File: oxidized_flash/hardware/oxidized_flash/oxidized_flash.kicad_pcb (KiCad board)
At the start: 2 copper layers, 61 x 21.6 mm, 20 parts, among them J1 USB_A, J2 Conn_ARM_JTAG_SWD_10, U1 LM1117-3.3, U2 ATSAMD51G18A-MU, U3 MT25QL

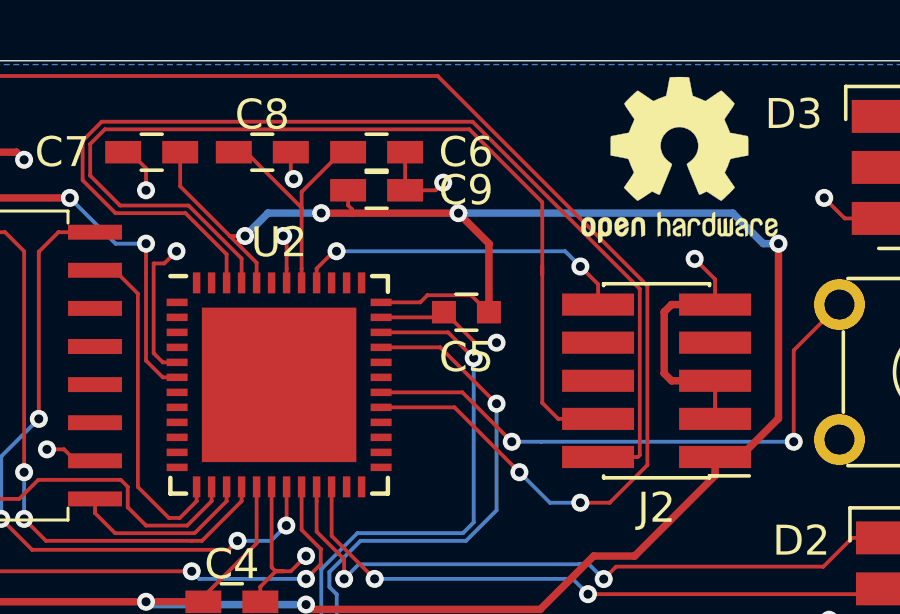
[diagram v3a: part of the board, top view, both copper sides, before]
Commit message: Update C5 to use a hand-soldered footprint
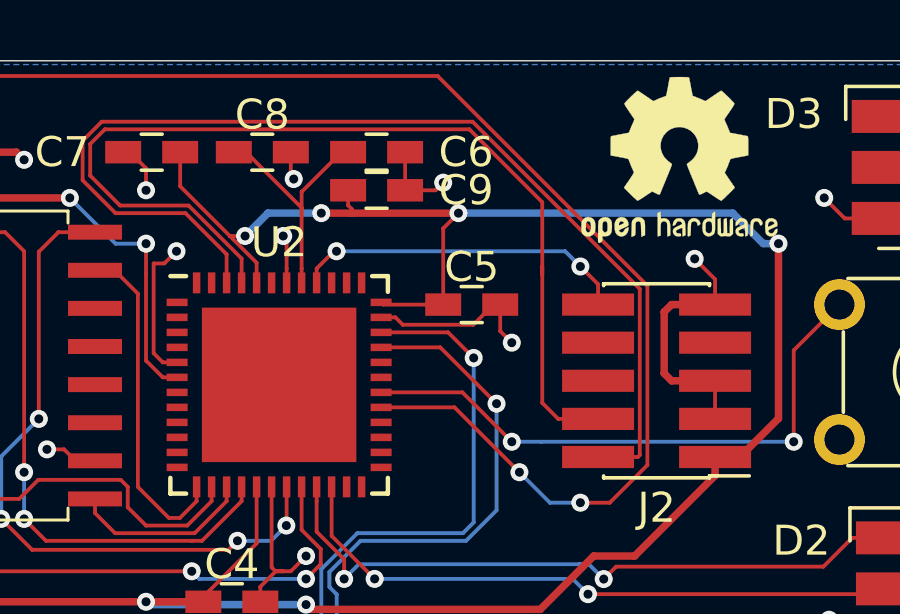
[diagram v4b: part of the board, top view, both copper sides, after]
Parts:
- C5: footprint Capacitors_SMD:C_0603 -> Capacitors_SMD:C_0603_HandSoldering
- moved C5 0.31 mm to (63.4, 28.4), turned to 0 degrees
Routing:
- net +3V3: track 132.9 -> 130.6 mm
- net GND: track 54.2 -> 55.6 mm
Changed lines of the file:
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@@
     (thickness 1.6)
     (drawings 6)
-    (tracks 380)
+    (tracks 379)
     (zones 0)
     (modules 20)
@@
       (xy -0.113933 -2.757629) (xy -0.013056 -2.757714) (xy 0 -2.757714) (xy 0.10391 -2.757652)) (layer F.SilkS) (width 0.01))
   )
-  (module Capacitors_SMD:C_0603 (layer F.Cu)
-    (at 63.258 28.702 180)
-    (descr "Capacitor SMD 0603, reflow soldering, AVX (see smccp.pdf)")
-    (tags "capacitor 0603")
-    (attr smd)
-    (fp_text reference C5 (at 0 -1.5) (layer F.SilkS)
-      (effects (font (size 1 1) (thickness 0.15)))
-    )
-    (fp_text value 10u (at 0 1.5) (layer F.Fab)
-      (effects (font (size 1 1) (thickness 0.15)))
-    )
-    (fp_text user %R (at 0 0) (layer F.Fab)
-      (effects (font (size 0.3 0.3) (thickness 0.075)))
-    )
-    (fp_line (start -0.8 0.4) (end -0.8 -0.4) (layer F.Fab) (width 0.1))
-    (fp_line (start 0.8 0.4) (end -0.8 0.4) (layer F.Fab) (width 0.1))
-    (fp_line (start 0.8 -0.4) (end 0.8 0.4) (layer F.Fab) (width 0.1))
-    (fp_line (start -0.8 -0.4) (end 0.8 -0.4) (layer F.Fab) (width 0.1))
-    (fp_line (start -0.35 -0.6) (end 0.35 -0.6) (layer F.SilkS) (width 0.12))
-    (fp_line (start 0.35 0.6) (end -0.35 0.6) (layer F.SilkS) (width 0.12))
-    (fp_line (start -1.4 -0.65) (end 1.4 -0.65) (layer F.CrtYd) (width 0.05))
-    (fp_line (start -1.4 -0.65) (end -1.4 0.65) (layer F.CrtYd) (width 0.05))
-    (fp_line (start 1.4 0.65) (end 1.4 -0.65) (layer F.CrtYd) (width 0.05))
-    (fp_line (start 1.4 0.65) (end -1.4 0.65) (layer F.CrtYd) (width 0.05))
-    (pad 1 smd rect (at -0.75 0 180) (size 0.8 0.75) (layers F.Cu F.Paste F.Mask)
-      (net 3 +3V3))
-    (pad 2 smd rect (at 0.75 0 180) (size 0.8 0.75) (layers F.Cu F.Paste F.Mask)
-      (net 1 GND))
-    (model Capacitors_SMD.3dshapes/C_0603.wrl
-      (at (xyz 0 0 0))
-      (scale (xyz 1 1 1))
-      (rotate (xyz 0 0 0))
-    )
-  )
   (module Pin_Headers:Pin_Header_Straight_2x05_Pitch1.27mm_SMD (layer F.Cu)
     (at 69.596 30.988 180)
@@
     )
   )
+  (module Capacitors_SMD:C_0603_HandSoldering (layer F.Cu)
+    (at 63.434 28.448)
+    (descr "Capacitor SMD 0603, hand soldering")
+    (tags "capacitor 0603")
+    (attr smd)
+    (fp_text reference C5 (at 0 -1.25) (layer F.SilkS)
+      (effects (font (size 1 1) (thickness 0.15)))
+    )
+    (fp_text value 10u (at 0 1.5) (layer F.Fab)
+      (effects (font (size 1 1) (thickness 0.15)))
+    )
+    (fp_line (start 1.8 0.65) (end -1.8 0.65) (layer F.CrtYd) (width 0.05))
+    (fp_line (start 1.8 0.65) (end 1.8 -0.65) (layer F.CrtYd) (width 0.05))
+    (fp_line (start -1.8 -0.65) (end -1.8 0.65) (layer F.CrtYd) (width 0.05))
+    (fp_line (start -1.8 -0.65) (end 1.8 -0.65) (layer F.CrtYd) (width 0.05))
+    (fp_line (start 0.35 0.6) (end -0.35 0.6) (layer F.SilkS) (width 0.12))
+    (fp_line (start -0.35 -0.6) (end 0.35 -0.6) (layer F.SilkS) (width 0.12))
+    (fp_line (start -0.8 -0.4) (end 0.8 -0.4) (layer F.Fab) (width 0.1))
+    (fp_line (start 0.8 -0.4) (end 0.8 0.4) (layer F.Fab) (width 0.1))
+    (fp_line (start 0.8 0.4) (end -0.8 0.4) (layer F.Fab) (width 0.1))
+    (fp_line (start -0.8 0.4) (end -0.8 -0.4) (layer F.Fab) (width 0.1))
+    (fp_text user %R (at 0 -1.25) (layer F.Fab)
+      (effects (font (size 1 1) (thickness 0.15)))
+    )
+    (pad 2 smd rect (at 0.95 0) (size 1.2 0.75) (layers F.Cu F.Paste F.Mask)
+      (net 1 GND))
+    (pad 1 smd rect (at -0.95 0) (size 1.2 0.75) (layers F.Cu F.Paste F.Mask)
+      (net 3 +3V3))
+    (model Capacitors_SMD.3dshapes/C_0603.wrl
+      (at (xyz 0 0 0))
+      (scale (xyz 1 1 1))
+      (rotate (xyz 0 0 0))
+    )
+  )
   (gr_text "Oxidized Flash Rev. 2" (at 67.564 40.132) (layer F.SilkS)
     (effects (font (size 0.75 0.75) (thickness 0.1875)))
@@
   (segment (start 53.13725 30.37375) (end 52.832009 30.068509) (width 0.127) (layer F.Cu) (net 1))
   (segment (start 53.61425 30.37375) (end 53.13725 30.37375) (width 0.127) (layer F.Cu) (net 1))
-  (segment (start 62.33625 28.87375) (end 62.508 28.702) (width 0.127) (layer F.Cu) (net 1))
-  (segment (start 60.41425 28.87375) (end 62.33625 28.87375) (width 0.127) (layer F.Cu) (net 1))
   (segment (start 57.26425 27.24675) (end 57.26425 27.72375) (width 0.127) (layer F.Cu) (net 1))
   (segment (start 57.26425 26.21925) (end 57.26425 27.24675) (width 0.127) (layer F.Cu) (net 1))
-  (via (at 64.262 29.718) (size 0.6) (drill 0.3) (layers F.Cu B.Cu) (net 1))
-  (segment (start 63.549 29.718) (end 64.262 29.718) (width 0.127) (layer F.Cu) (net 1))
-  (segment (start 62.508 28.702) (end 62.533 28.702) (width 0.127) (layer F.Cu) (net 1))
-  (segment (start 62.533 28.702) (end 63.549 29.718) (width 0.127) (layer F.Cu) (net 1))
   (via (at 75.347522 38.952478) (size 0.6) (drill 0.3) (layers F.Cu B.Cu) (net 1))
   (segment (start 77.242 39.624) (end 76.019044 39.624) (width 0.25) (layer F.Cu) (net 1))
@@
   (segment (start 61.214 24.638) (end 62.23 24.638) (width 0.127) (layer F.Cu) (net 1))
   (segment (start 62.23 24.638) (end 62.484 24.384) (width 0.127) (layer F.Cu) (net 1))
+  (segment (start 64.159 28.448) (end 64.384 28.448) (width 0.127) (layer F.Cu) (net 1))
+  (segment (start 63.48726 29.11974) (end 64.159 28.448) (width 0.127) (layer F.Cu) (net 1))
+  (segment (start 61.13724 29.11974) (end 63.48726 29.11974) (width 0.127) (layer F.Cu) (net 1))
+  (segment (start 60.89125 28.87375) (end 61.13724 29.11974) (width 0.127) (layer F.Cu) (net 1))
+  (segment (start 60.41425 28.87375) (end 60.89125 28.87375) (width 0.127) (layer F.Cu) (net 1))
+  (via (at 64.77 29.718) (size 0.6) (drill 0.3) (layers F.Cu B.Cu) (net 1))
+  (segment (start 64.384 28.448) (end 64.384 29.332) (width 0.127) (layer F.Cu) (net 1))
+  (segment (start 64.384 29.332) (end 64.77 29.718) (width 0.127) (layer F.Cu) (net 1))
   (segment (start 58.841 26.67) (end 58.928 26.67) (width 0.127) (layer F.Cu) (net 2))
   (segment (start 58.26425 27.72375) (end 58.26425 27.24675) (width 0.127) (layer F.Cu) (net 2))
@@
   (segment (start 55.88 26.162) (end 55.373 26.162) (width 0.127) (layer F.Cu) (net 3))
   (segment (start 56.26425 27.05325) (end 55.3725 26.1615) (width 0.127) (layer F.Cu) (net 3))
-  (segment (start 63.417499 28.136499) (end 63.983 28.702) (width 0.127) (layer F.Cu) (net 3))
-  (segment (start 61.955599 28.136499) (end 63.417499 28.136499) (width 0.127) (layer F.Cu) (net 3))
-  (segment (start 61.718348 28.37375) (end 61.955599 28.136499) (width 0.127) (layer F.Cu) (net 3))
-  (segment (start 60.41425 28.37375) (end 61.718348 28.37375) (width 0.127) (layer F.Cu) (net 3))
-  (segment (start 63.983 28.702) (end 64.008 28.702) (width 0.127) (layer F.Cu) (net 3))
-  (segment (start 64.008 26.416) (end 62.992 25.4) (width 0.25) (layer F.Cu) (net 3))
-  (segment (start 64.008 28.702) (end 64.008 26.416) (width 0.25) (layer F.Cu) (net 3))
   (segment (start 36.322 27.936) (end 36.326 27.936) (width 0.25) (layer F.Cu) (net 3))
   (segment (start 36.957 27.305) (end 41.578 27.305) (width 0.25) (layer F.Cu) (net 3))
@@
   (segment (start 62.992 25.4) (end 59.436 25.4) (width 0.25) (layer F.Cu) (net 3))
   (segment (start 59.436 25.4) (end 58.42 25.4) (width 0.25) (layer F.Cu) (net 3))
+  (segment (start 62.484 25.908) (end 62.484 28.448) (width 0.127) (layer F.Cu) (net 3))
+  (segment (start 62.992 25.4) (end 62.484 25.908) (width 0.127) (layer F.Cu) (net 3))
+  (segment (start 60.4885 28.448) (end 60.41425 28.37375) (width 0.127) (layer F.Cu) (net 3))
+  (segment (start 62.484 28.448) (end 60.4885 28.448) (width 0.127) (layer F.Cu) (net 3))
   (segment (start 57.76425 27.24675) (end 57.76425 27.72375) (width 0.127) (layer F.Cu) (net 4))
   (segment (start 57.76425 25.21925) (end 57.76425 25.50625) (width 0.127) (layer F.Cu) (net 4))

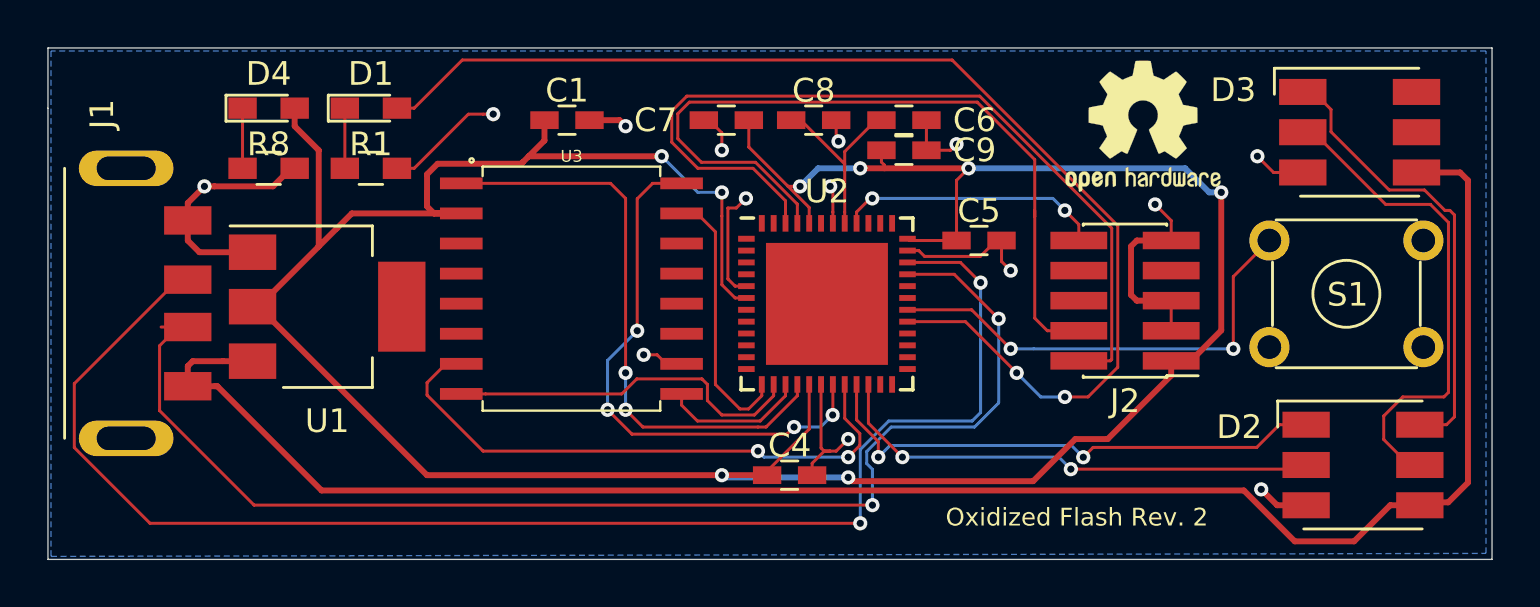
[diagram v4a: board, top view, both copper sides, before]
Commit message: Don't couple power rail to the JTAG connector
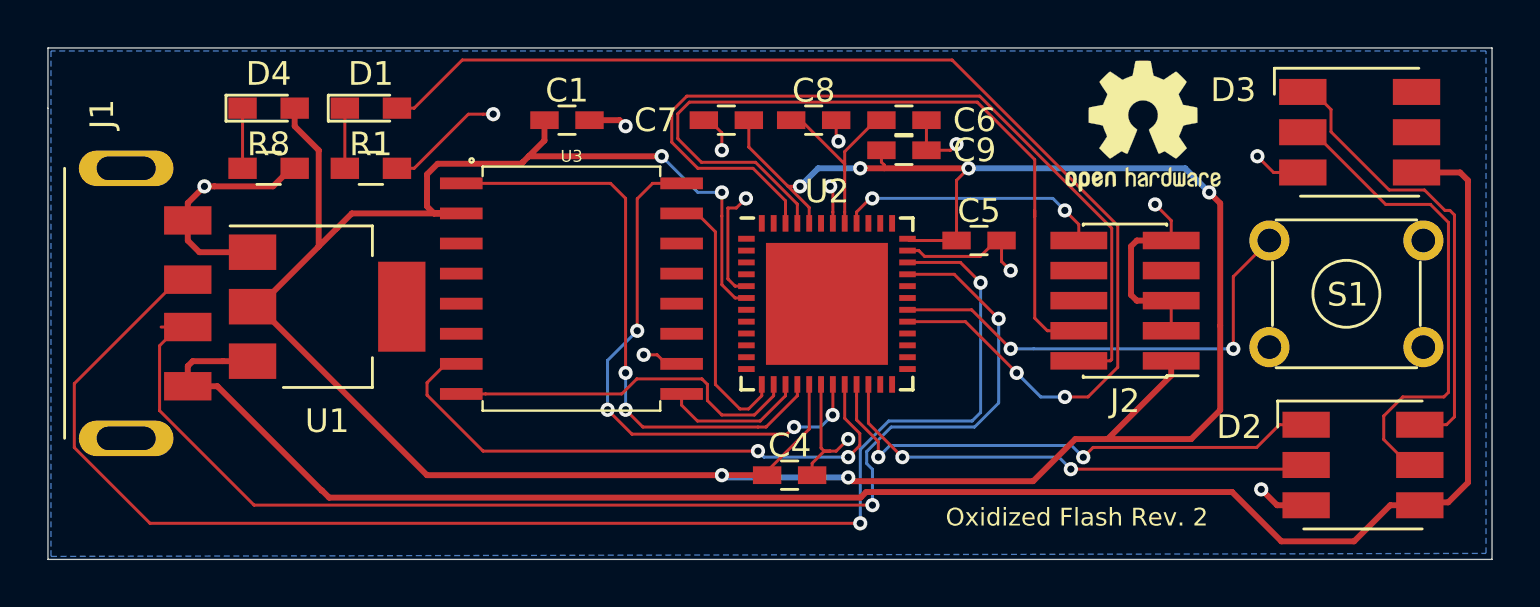
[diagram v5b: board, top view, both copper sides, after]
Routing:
- net +3V3: track 130.6 -> 137.1 mm
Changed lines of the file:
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@@
     (thickness 1.6)
     (drawings 6)
-    (tracks 379)
+    (tracks 384)
     (zones 0)
     (modules 20)
@@
   )
   (setup
-    (last_trace_width 0.127)
+    (last_trace_width 0.25)
     (user_trace_width 0.127)
     (trace_clearance 0.127)
@@
   (segment (start 67.056 27.178) (end 67.646 27.768) (width 0.127) (layer F.Cu) (net 2))
   (segment (start 56.26425 27.72375) (end 56.26425 27.05325) (width 0.127) (layer F.Cu) (net 3))
-  (segment (start 72.376 33.528) (end 73.66 32.244) (width 0.25) (layer F.Cu) (net 3))
   (segment (start 71.546 33.528) (end 72.376 33.528) (width 0.25) (layer F.Cu) (net 3))
-  (via (at 73.66 26.416) (size 0.6) (drill 0.3) (layers F.Cu B.Cu) (net 3))
-  (segment (start 73.66 32.244) (end 73.66 26.416) (width 0.25) (layer F.Cu) (net 3))
-  (segment (start 73.66 26.416) (end 73.152 26.416) (width 0.25) (layer B.Cu) (net 3))
   (via (at 62.992 25.4) (size 0.6) (drill 0.3) (layers F.Cu B.Cu) (net 3))
   (segment (start 73.152 26.416) (end 72.136 25.4) (width 0.25) (layer B.Cu) (net 3))
@@
   (segment (start 60.4885 28.448) (end 60.41425 28.37375) (width 0.127) (layer F.Cu) (net 3))
   (segment (start 62.484 28.448) (end 60.4885 28.448) (width 0.127) (layer F.Cu) (net 3))
+  (segment (start 68.864 36.83) (end 72.39 36.83) (width 0.25) (layer F.Cu) (net 3))
+  (segment (start 72.39 36.83) (end 73.615999 35.604001) (width 0.25) (layer F.Cu) (net 3))
+  (segment (start 73.615999 35.604001) (end 73.615999 32.048001) (width 0.25) (layer F.Cu) (net 3))
+  (via (at 73.152 26.416) (size 0.6) (drill 0.3) (layers F.Cu B.Cu) (net 3))
+  (segment (start 73.615999 32.048001) (end 73.615999 26.879999) (width 0.25) (layer F.Cu) (net 3))
+  (segment (start 73.615999 26.879999) (end 73.152 26.416) (width 0.25) (layer F.Cu) (net 3))
   (segment (start 57.76425 27.24675) (end 57.76425 27.72375) (width 0.127) (layer F.Cu) (net 4))
   (segment (start 57.76425 25.21925) (end 57.76425 25.50625) (width 0.127) (layer F.Cu) (net 4))
@@
   (segment (start 80.6 26.924) (end 82.48847 26.924) (width 0.127) (layer F.Cu) (net 9))
   (segment (start 82.48847 26.924) (end 83.25047 27.686) (width 0.127) (layer F.Cu) (net 9))
-  (segment (start 31.282 34.6) (end 35.682 39) (width 0.25) (layer F.Cu) (net 10))
-  (segment (start 30.032 34.6) (end 31.186 34.6) (width 0.25) (layer F.Cu) (net 10))
-  (segment (start 31.186 34.6) (end 31.282 34.6) (width 0.25) (layer F.Cu) (net 10))
-  (segment (start 74.614398 39) (end 76.762398 41.148) (width 0.25) (layer F.Cu) (net 10))
-  (segment (start 35.682 39) (end 74.614398 39) (width 0.25) (layer F.Cu) (net 10))
-  (segment (start 80.792 39.624) (end 82.042 39.624) (width 0.25) (layer F.Cu) (net 10))
-  (segment (start 79.268 41.148) (end 80.792 39.624) (width 0.25) (layer F.Cu) (net 10))
-  (segment (start 76.762398 41.148) (end 79.268 41.148) (width 0.25) (layer F.Cu) (net 10))
   (segment (start 82.352 25.576) (end 81.902 25.576) (width 0.25) (layer F.Cu) (net 10))
   (segment (start 84.074 25.908) (end 83.742 25.576) (width 0.25) (layer F.Cu) (net 10))
@@
   (segment (start 41.621 20.828) (end 62.298126 20.828) (width 0.127) (layer F.Cu) (net 5))
   (segment (start 36.662 25.4) (end 36.662 22.86) (width 0.127) (layer F.Cu) (net 6))
+  (segment (start 80.792 39.624) (end 82.042 39.624) (width 0.25) (layer F.Cu) (net 10))
+  (segment (start 74.117931 39.065931) (end 76.2 41.148) (width 0.25) (layer F.Cu) (net 10))
+  (segment (start 58.669107 39.065931) (end 74.117931 39.065931) (width 0.25) (layer F.Cu) (net 10))
+  (segment (start 76.2 41.148) (end 79.268 41.148) (width 0.25) (layer F.Cu) (net 10))
+  (segment (start 58.432616 39.302422) (end 58.669107 39.065931) (width 0.25) (layer F.Cu) (net 10))
+  (segment (start 31.282 34.6) (end 35.682 39) (width 0.25) (layer F.Cu) (net 10))
+  (segment (start 79.268 41.148) (end 80.792 39.624) (width 0.25) (layer F.Cu) (net 10))
+  (segment (start 30.032 34.6) (end 31.282 34.6) (width 0.25) (layer F.Cu) (net 10))
+  (segment (start 35.682 39) (end 35.698 39) (width 0.25) (layer F.Cu) (net 10))
+  (segment (start 35.698 39) (end 36.000422 39.302422) (width 0.25) (layer F.Cu) (net 10))
+  (segment (start 36.000422 39.302422) (end 58.432616 39.302422) (width 0.25) (layer F.Cu) (net 10))
   (segment (start 32.344 25.4) (end 32.344 22.86) (width 0.127) (layer F.Cu) (net 14))
   (via (at 64.262 31.75) (size 0.6) (drill 0.3) (layers F.Cu B.Cu) (net 15))
